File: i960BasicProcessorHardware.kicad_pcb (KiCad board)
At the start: 4 copper layers, 169.9 x 169.8 mm, 67 parts, among them J1 Conn_01x08, J10 Conn_01x03, J11 Conn_01x08, J2 Conn_02x39_Odd_Even, J3 Conn_01x03, J4 Conn_02x05_Odd_Even, J5 Conn_02x05_Odd_Even, J6 Conn_02x05_Odd_Even, J7 Conn_01x06, J8 Conn_01x06, J9 Conn_01x12, SW1 SW_Push, U1 74HC245, U10 74LS08, U11 74LS04, U12 74LS174, U13 SN74LVC245AN, U14 74LS174, U15 MCP23S17_SP, U16 MCP23S17_SP, U17 MCP23S17_SP, U18 ATtiny85-20PU, U2 80960Sx, U3 MCP23S17_SP, U4 74HC245, U5 74HC573, U6 74HC573, U7 Adafruit_FeatherWing (PSRAM F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, U8 Adafruit_FeatherWing (PSRAM F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, U9 74LS125

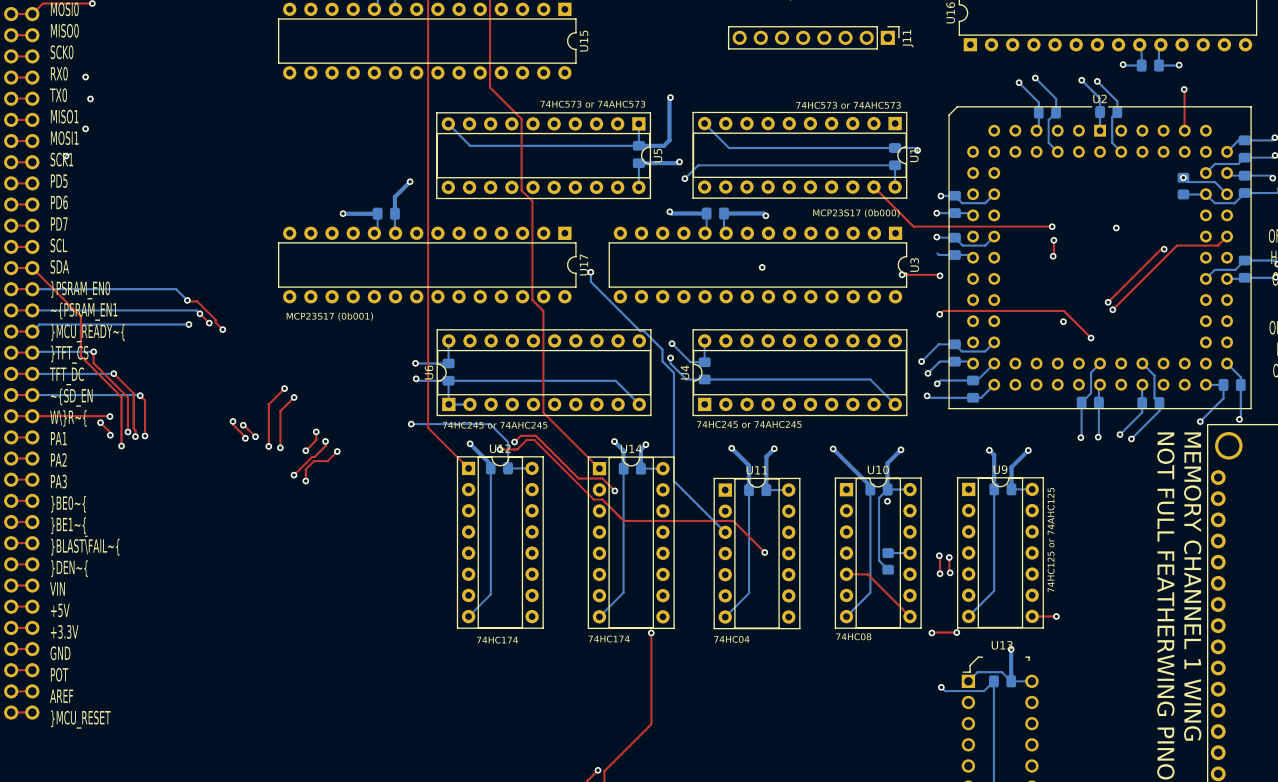
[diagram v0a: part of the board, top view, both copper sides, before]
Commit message: Upper 8 breakout successfully routed in
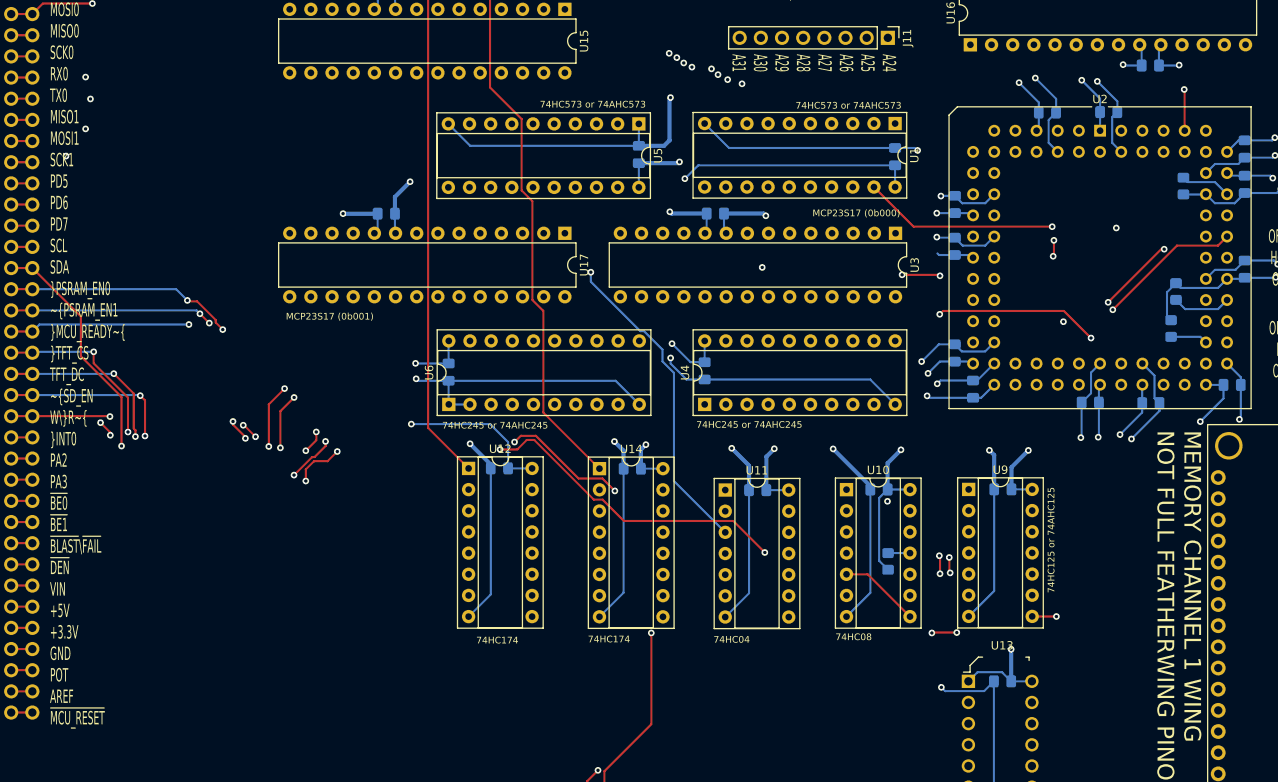
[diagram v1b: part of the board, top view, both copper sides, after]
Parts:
- added R3: 10k, Resistor_SMD:R_0805_2012Metric_Pad1.20x1.40mm_HandSolder, B.Cu at (158.8, 78.0)
- added R5: 10k, Resistor_SMD:R_0805_2012Metric_Pad1.20x1.40mm_HandSolder, B.Cu at (158.2, 82.4)
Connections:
- RN1 pad 2: /~INT3 -> Net-(RN1-Pad2)
- RN1 pad 3: /~INT0 -> Net-(RN1-Pad3)
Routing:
- net /A24: track 63.7 -> 83.9 mm, vias 0 -> 1
- net /A25: track 68.7 -> 88.1 mm, vias 0 -> 1
- net /A26: track 76.2 -> 93.9 mm, vias 0 -> 1
- net /A27: track 77.1 -> 92.8 mm, vias 0 -> 1
- net /A28: track 85.2 -> 100.7 mm, vias 0 -> 1
- net /A29: track 92.7 -> 106.4 mm, vias 0 -> 1
- net +5V: track 271.2 -> 283.1 mm
- net /A30: track 93.6 -> 105.3 mm, vias 0 -> 1
- net /A31: track 101.1 -> 110.7 mm, vias 0 -> 1
- net /~INT3: track 24.1 -> 31.2 mm
- net /~INT0: track 2.54 -> 6.99 mm
- net /~LOCK: vias 1 -> 0
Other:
- board text added: "A24 A25 A26 A27 A28 A29 A30 A31"
- board text added: "FAIL CLKO PB2 PB3 ~GPIO_CS MOSI0 MISO0 SCK0 RX0 TX0 MISO1 MOSI1 SCK1 PD5 PD6 PD7 SCL SDA ~PSRAM_EN0 ~PSRAM_EN1 ~MCU_READY~ ~TFT_CS TFT_DC ~SD_EN W\~R~ ~INT0 PA2 PA3 ~BE0~ ~BE1~ ~BLAST~\~FAIL~ ~DEN~ VIN +5V +3.3V GND POT AREF ~MCU_RESET~"
- board text removed: "FAIL CLKO PB2 PB3 ~GPIO_CS MOSI0 MISO0 SCK0 RX0 TX0 MISO1 MOSI1 SCK1 PD5 PD6 PD7 SCL SDA ~PSRAM_EN0 ~PSRAM_EN1 ~MCU_READY~ ~TFT_CS TFT_DC ~SD_EN W\~R~ PA1 PA2 PA3 ~BE0~ ~BE1~ ~BLAST~\~FAIL~ ~DEN~ VIN +5V +3.3V GND POT AREF ~MCU_RESET~"

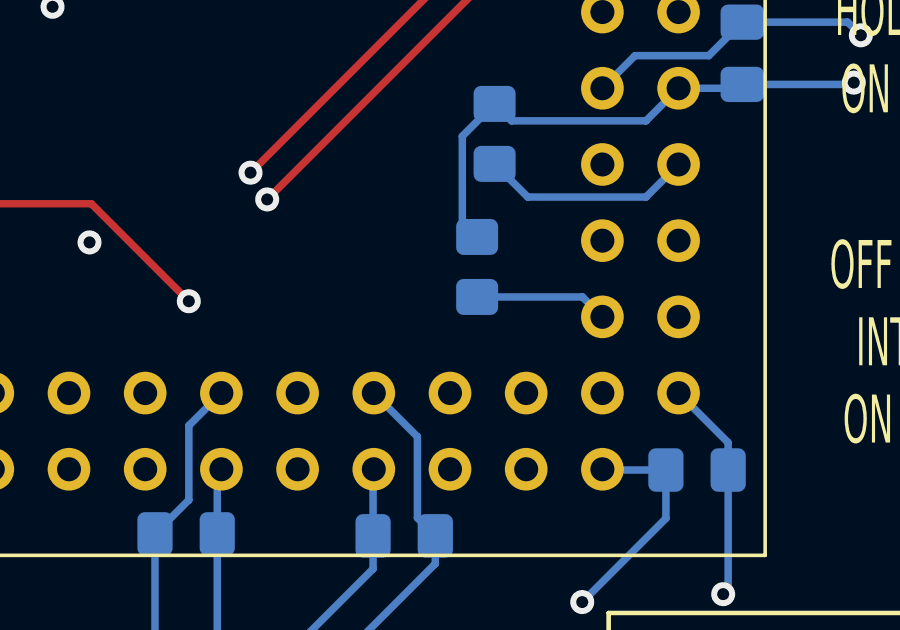
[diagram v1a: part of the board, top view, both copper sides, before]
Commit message: move ~RESET960 back to the primary chipset
also move ~INT3 to it as well. I want two different interrupt pins
accessible to the primary chipset. I have made the fourth ioexpander
completely exposed to the i960.
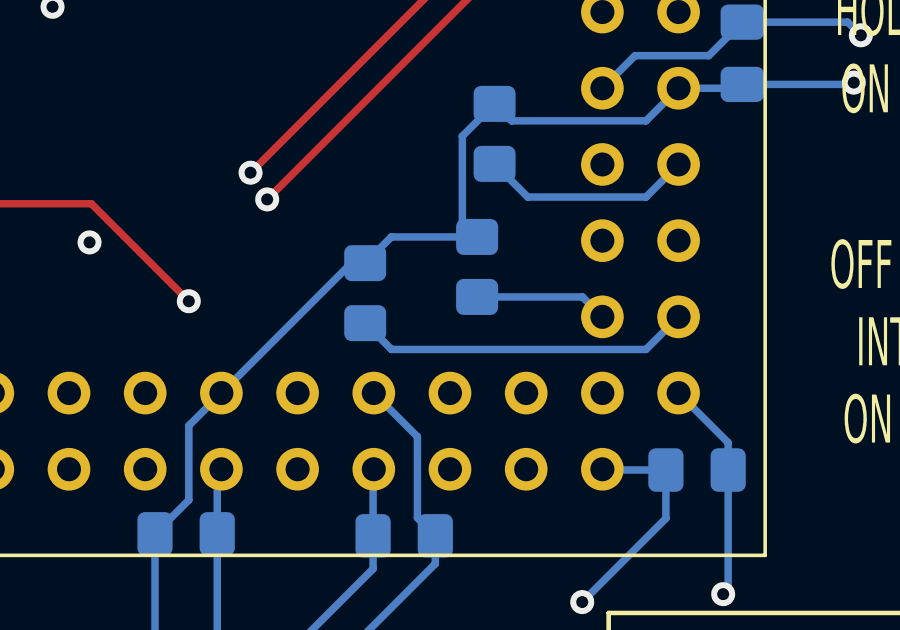
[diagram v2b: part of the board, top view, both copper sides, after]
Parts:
- added R6: 10k, Resistor_SMD:R_0805_2012Metric_Pad1.20x1.40mm_HandSolder, B.Cu at (154.5, 83.3)
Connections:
- RN1 pad 7: /~RESET960 -> Net-(RN1-Pad7)
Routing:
- net /~RESET960: track 53.7 -> 64.9 mm
- net +5V: track 283.1 -> 293.8 mm

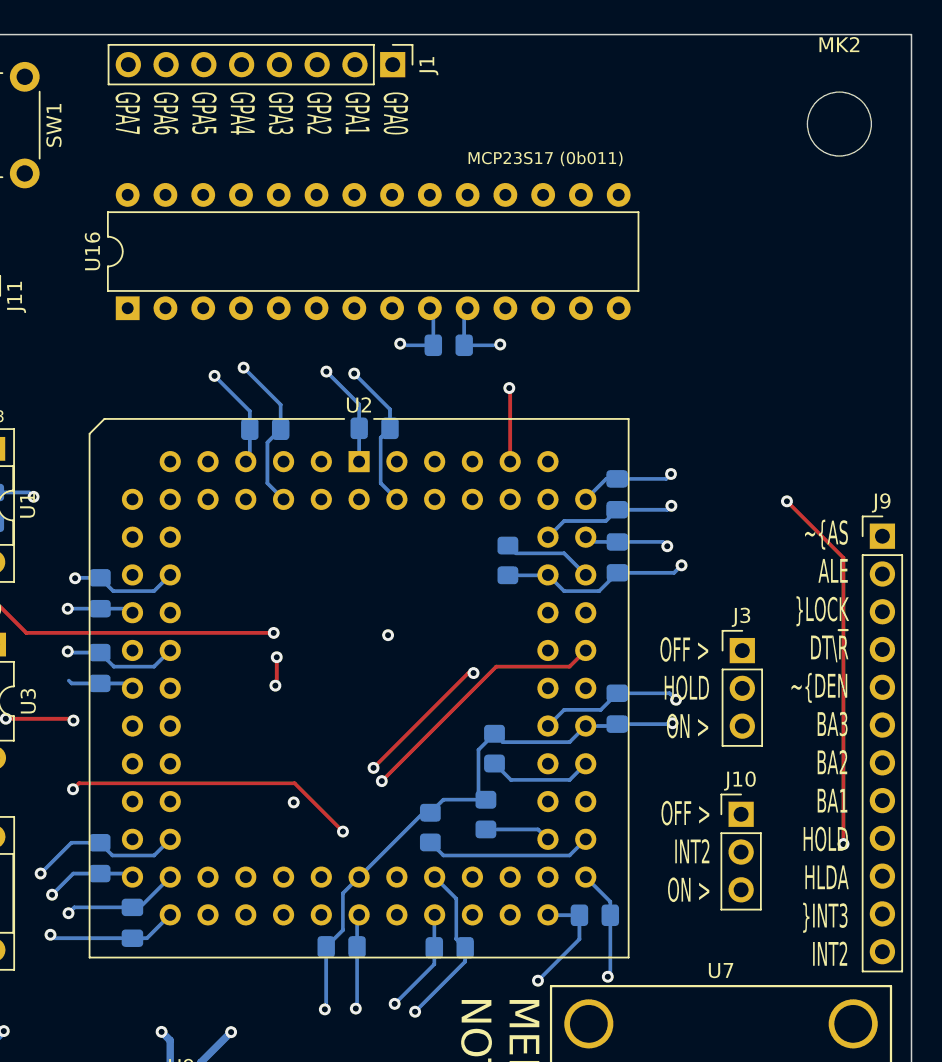
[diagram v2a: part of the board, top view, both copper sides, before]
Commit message: Wireup the fourth gpio expander
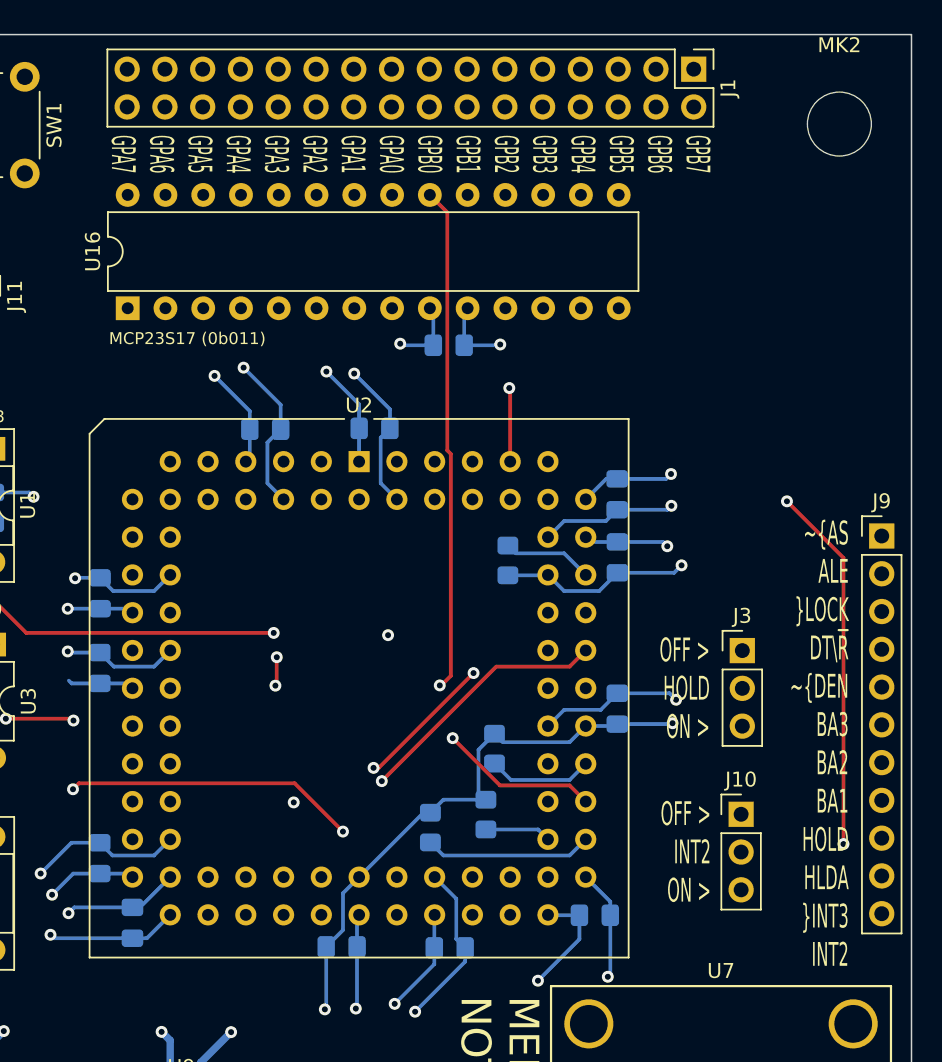
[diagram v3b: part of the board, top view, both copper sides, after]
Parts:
- J1: value Conn_01x08 -> Conn_02x16_Odd_Even; footprint Connector_PinHeader_2.54mm:PinHeader_1x08_P2.54mm_Vertical -> Connector_PinHeader_2.54mm:PinHeader_2x16_P2.54mm_Vertical
- J9: value Conn_01x12 -> Conn_01x11; footprint Connector_PinHeader_2.54mm:PinHeader_1x12_P2.54mm_Vertical -> Connector_PinHeader_2.54mm:PinHeader_1x11_P2.54mm_Vertical
- moved J1 20.2 mm to (172.2, 32.3)
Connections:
- J1 pad 1: /GPA0 -> /GPB7
- J1 pad 2: /GPA1 -> /GPB7
- J1 pad 3: /GPA2 -> /GPB6
- J1 pad 4: /GPA3 -> /GPB6
- J1 pad 5: /GPA4 -> /GPB5
- J1 pad 6: /GPA5 -> /GPB5
- J1 pad 7: /GPA6 -> /GPB4
- J1 pad 8: /GPA7 -> /GPB4
- J2 pad 53: /PA2 -> /~INT3
- J2 pad 54: /PA2 -> /~INT3
- J2 pad 55: /PA3 -> /~RESET960
- J2 pad 56: /PA3 -> /~RESET960
- J9 pad 11: /~INT3 -> /INT2_BREAKOUT
- U16 pad 1: /~RESET960 -> /GPB0
- U16 pad 2: Net-(U16-Pad2) -> /GPB1
- U16 pad 3: Net-(U16-Pad3) -> /GPB2
- U16 pad 4: Net-(U16-Pad4) -> /GPB3
- U16 pad 5: Net-(U16-Pad5) -> /GPB4
- U16 pad 6: Net-(U16-Pad6) -> /GPB5
- U16 pad 7: Net-(U16-Pad7) -> /GPB6
- U16 pad 8: Net-(U16-Pad8) -> /GPB7
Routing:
- net /INT1: track 0.00 -> 48.6 mm, vias 0 -> 2
- net /GPB1: track 0.00 -> 32.1 mm
- net /GPB3: track 0.00 -> 31.4 mm
- net /GPB6: track 0.00 -> 31.4 mm
- net /GPB4: track 0.00 -> 31.4 mm
- net /GPB5: track 0.00 -> 31.4 mm
- net /GPB2: track 0.00 -> 31.4 mm
- net /GPB0: track 0.00 -> 31.4 mm
- net /GPB7: track 0.00 -> 30.4 mm
- net /~INT3: track 31.2 -> 9.58 mm
- net /~RESET960: track 64.9 -> 67.5 mm
- net /PA3: track 2.54 -> 0.00 mm
- net /PA2: track 2.54 -> 0.00 mm
- net /INT2_BREAKOUT: track 11.2 -> 10.2 mm
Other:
- board text added: "GPB7 GPB6 GPB5 GPB4 GPB3 GPB2 GPB1 GPB0 GPA0 GPA1 GPA2 GPA3 GPA4 GPA5 GPA6 GPA7"
- board text removed: "GPA0 GPA1 GPA2 GPA3 GPA4 GPA5 GPA6 GPA7"

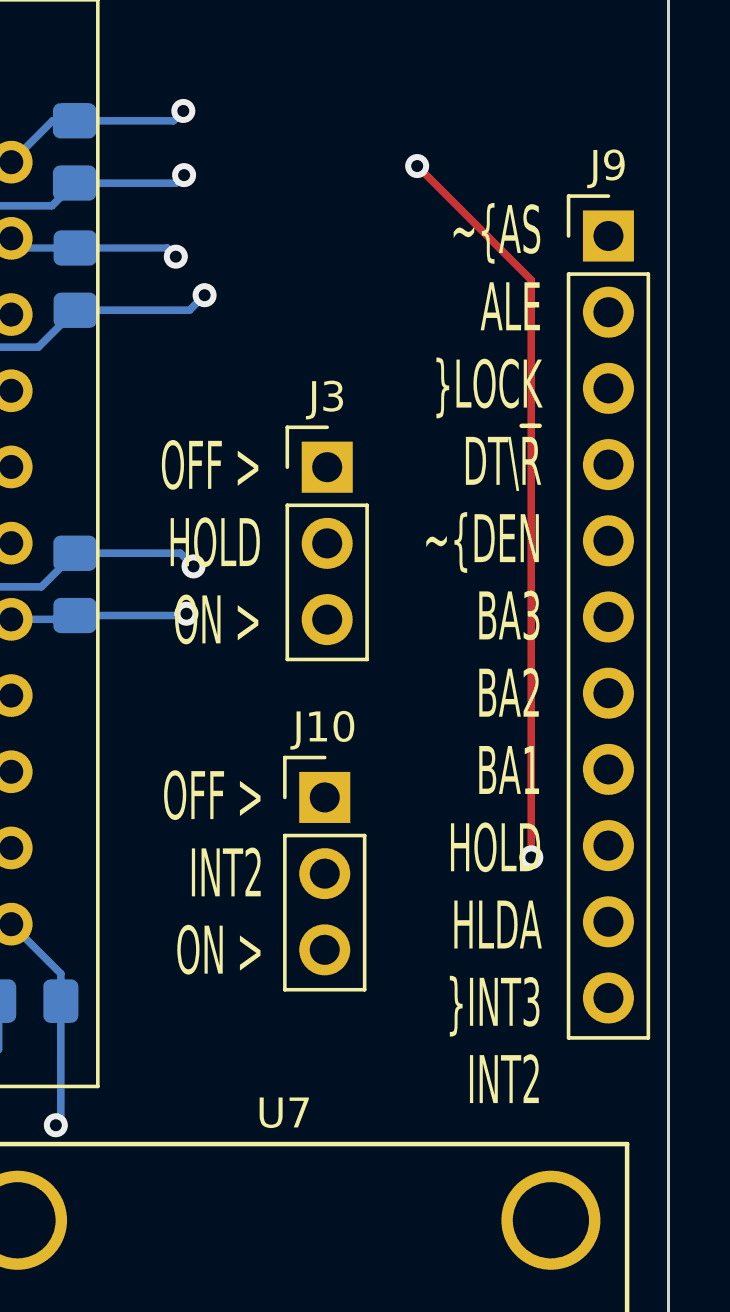
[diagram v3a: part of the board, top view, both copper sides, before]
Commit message: Update labels and delete bad trace
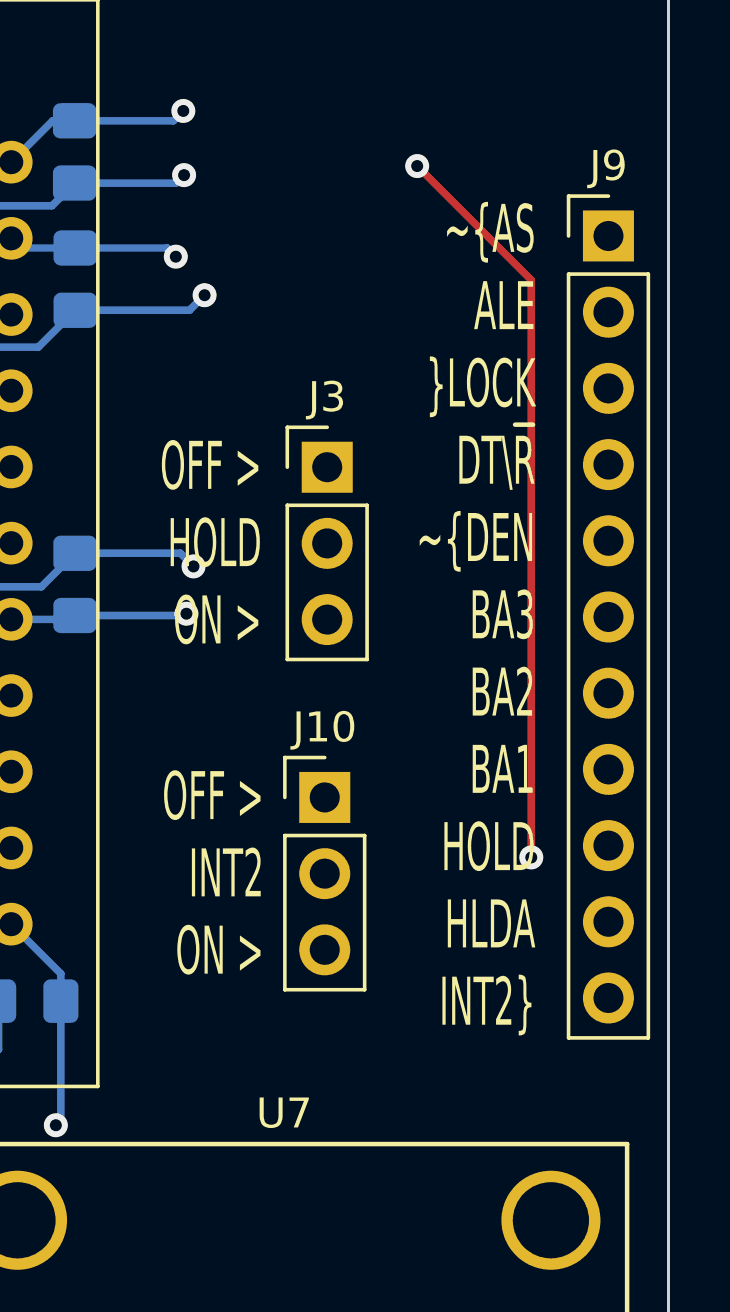
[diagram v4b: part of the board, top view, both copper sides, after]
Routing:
- net /~RESET960: track 67.5 -> 13.8 mm
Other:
- board text added: "~AS ALE ~LOCK DT\~R~ ~DEN BA3 BA2 BA1 HOLD HLDA INT2"
- board text removed: "~AS ALE ~LOCK DT\~R~ ~DEN BA3 BA2 BA1 HOLD HLDA ~INT3 INT2"
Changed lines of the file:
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@@
     (thickness 1.6)
     (drawings 39)
-    (tracks 1800)
+    (tracks 1793)
     (zones 0)
     (modules 70)
@@
     (effects (font (size 0.8 0.8) (thickness 0.1)))
   )
-  (gr_text "~AS\nALE\n~LOCK\nDT\\~R~\n~DEN\nBA3\nBA2\nBA1\nHOLD\nHLDA\n~INT3\nINT2" (at 182.63362 77.70622) (layer F.SilkS)
+  (gr_text "~AS\nALE\n~LOCK\nDT\\~R~\n~DEN\nBA3\nBA2\nBA1\nHOLD\nHLDA\nINT2" (at 182.41518 76.38034) (layer F.SilkS)
     (effects (font (size 1.6 0.8) (thickness 0.15)) (justify right))
   )
@@
   (segment (start 26.23857 58.972552) (end 29.735285 62.469267) (width 0.25) (layer In1.Cu) (net 5))
   (segment (start 26.23857 36.67797) (end 26.23857 58.972552) (width 0.25) (layer In1.Cu) (net 5))
-  (segment (start 144.732478 70.71534) (end 159.580497 85.563359) (width 0.25) (layer In2.Cu) (net 6))
-  (segment (start 163.486181 85.563359) (end 164.93998 84.10956) (width 0.25) (layer In2.Cu) (net 6))
-  (segment (start 140.626181 65.095001) (end 144.732478 69.201298) (width 0.25) (layer In2.Cu) (net 6))
-  (segment (start 159.580497 85.563359) (end 163.486181 85.563359) (width 0.25) (layer In2.Cu) (net 6))
-  (segment (start 144.732478 69.201298) (end 144.732478 70.71534) (width 0.25) (layer In2.Cu) (net 6))
-  (segment (start 140.626181 54.883401) (end 140.626181 65.095001) (width 0.25) (layer In2.Cu) (net 6))
-  (segment (start 134.1374 48.39462) (end 140.626181 54.883401) (width 0.25) (layer In2.Cu) (net 6))
   (segment (start 163.853779 85.195761) (end 164.93998 84.10956) (width 0.25) (layer Back) (net 6))
   (segment (start 155.369101 85.195761) (end 163.853779 85.195761) (width 0.25) (layer Back) (net 6))
